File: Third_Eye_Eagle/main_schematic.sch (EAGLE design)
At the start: 4 parts

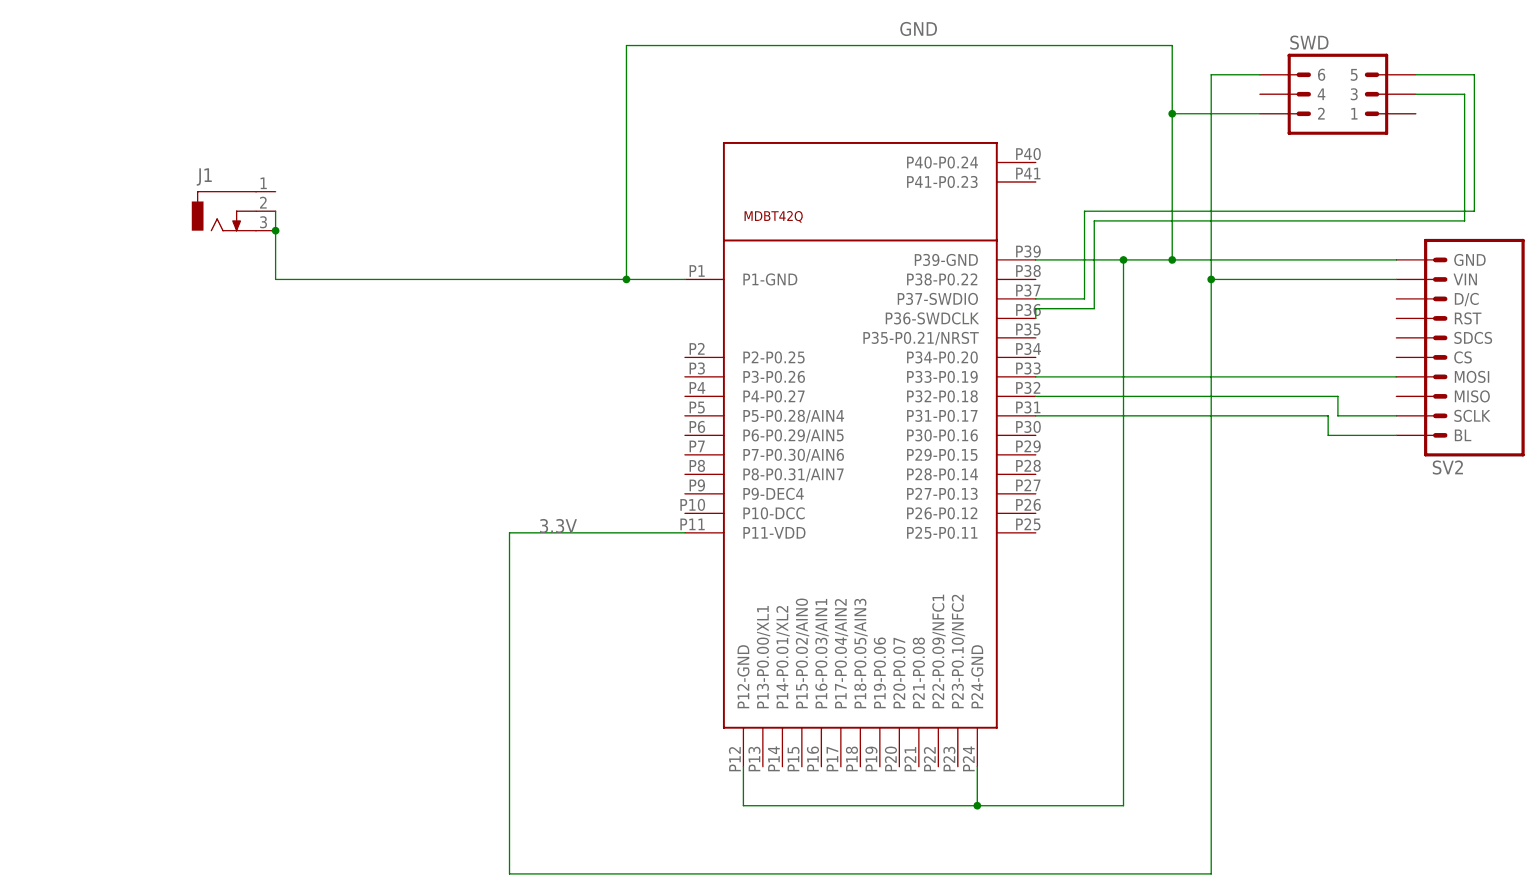
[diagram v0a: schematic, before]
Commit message: Alex additions to Eagle library and main schematic
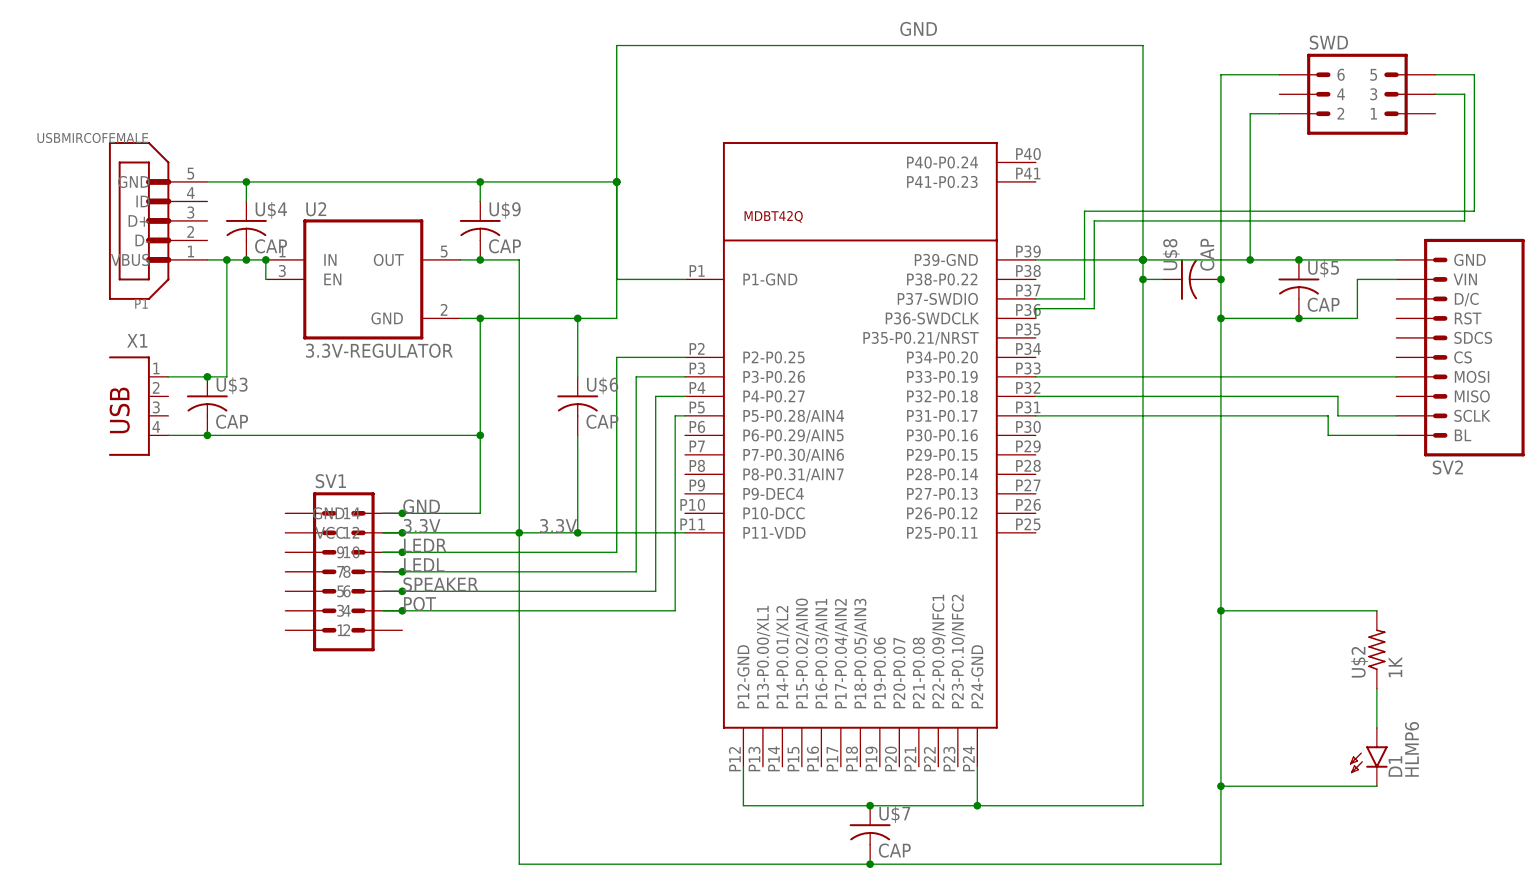
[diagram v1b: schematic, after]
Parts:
- removed J1: (no value), third_eye:DCJ0303
- added D1: HLMP6, display-hp:HLMP6
- added P1: USBMIRCOFEMALE, third_eye:USBMIRCOFEMALE
- added SV1: (no value), third_eye:MISCHEADER
- added U$2: 1K, third_eye:RESISTOR
- added U$3, U$4, U$5, U$6, U$7, U$8, U$9: CAP, third_eye:CAP
- added U2: 3.3V-REGULATOR, third_eye:3.3V-REGULATOR
- added X1: (no value), third_eye:USBCON
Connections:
- new net 5V: P1.VBUS, U$3.1, U$4.2, U2.EN, U2.IN, X1.1
- new net LEDL: SV1.7, U$1.P3-P0.26
- new net LEDR: SV1.9, U$1.P2-P0.25
- new net N$3: D1.A, U$2.1
- new net POT: SV1.3, U$1.P5-P0.28/AIN4
- new net SPEAKER: SV1.5, U$1.P4-P0.27
- net 3.3V: now also D1.K, SV1.VCC, U$2.2, U$5.2, U$6.2, U$7.2, U$8.2, U$9.2, U2.OUT
- net GND: now also P1.GND, SV1.GND, U$3.2, U$4.1, U$5.1, U$6.1, U$7.1, U$8.1, U$9.1, U2.GND, X1.4; no longer J1.2, J1.3
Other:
- moved on the sheet: SWD
